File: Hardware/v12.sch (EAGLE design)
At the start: 85 parts, among them IC1 LM324D, IC2 m328p, IC3 REG1117, IC4 OPA336U, J1 22-27-2081-08, J2 22-27-2031-03

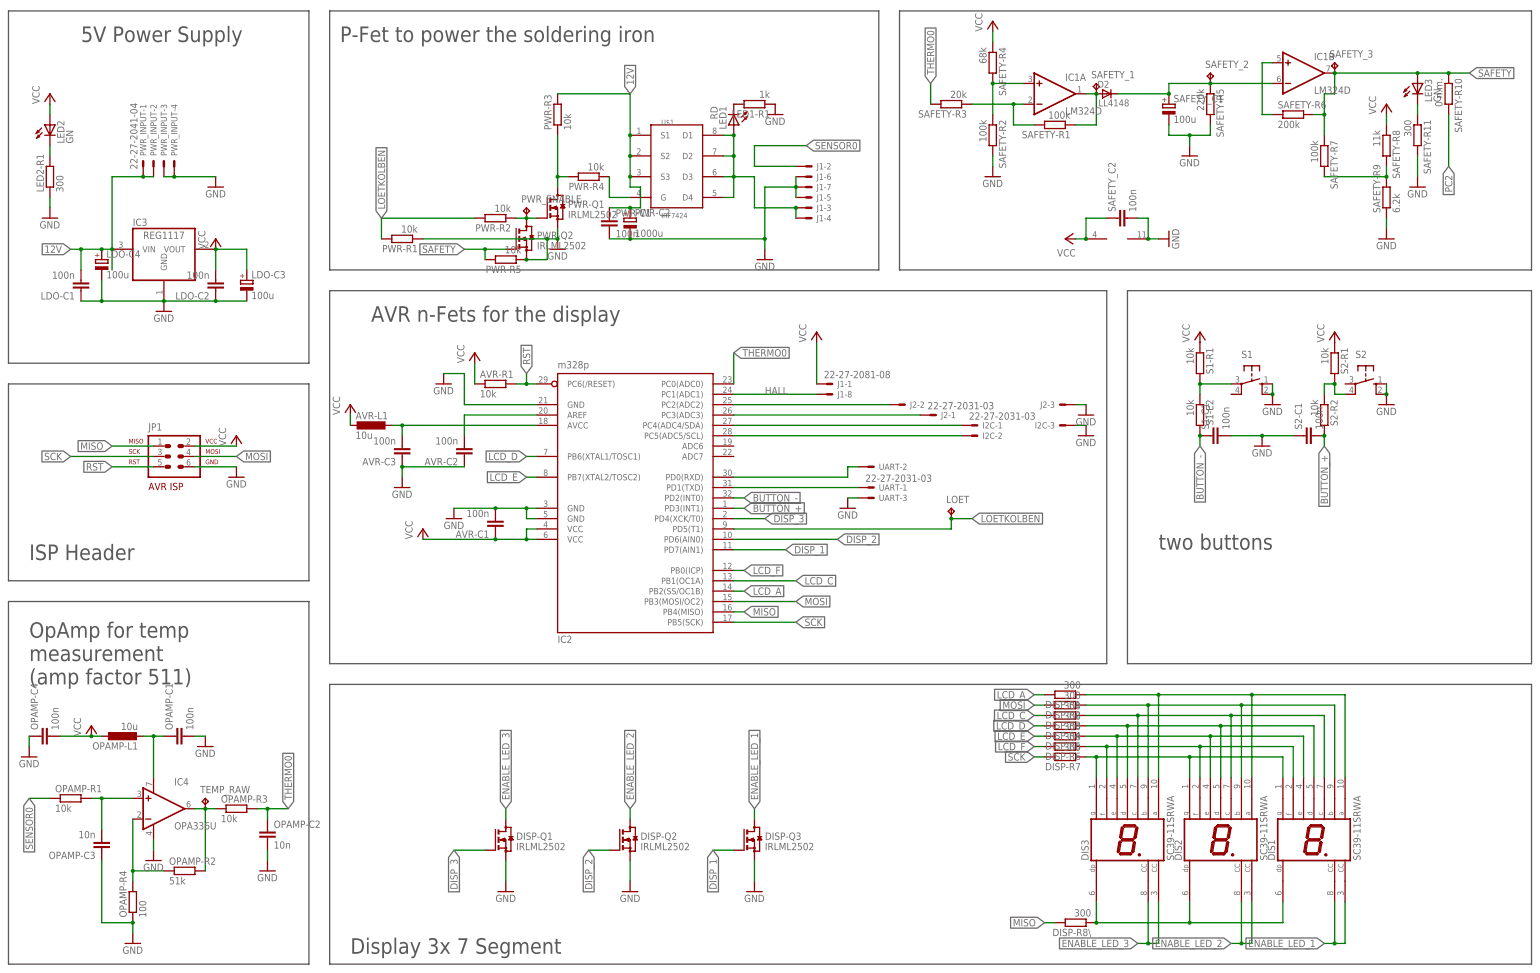
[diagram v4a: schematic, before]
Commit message: changed some values (led resistors) updated shopping list
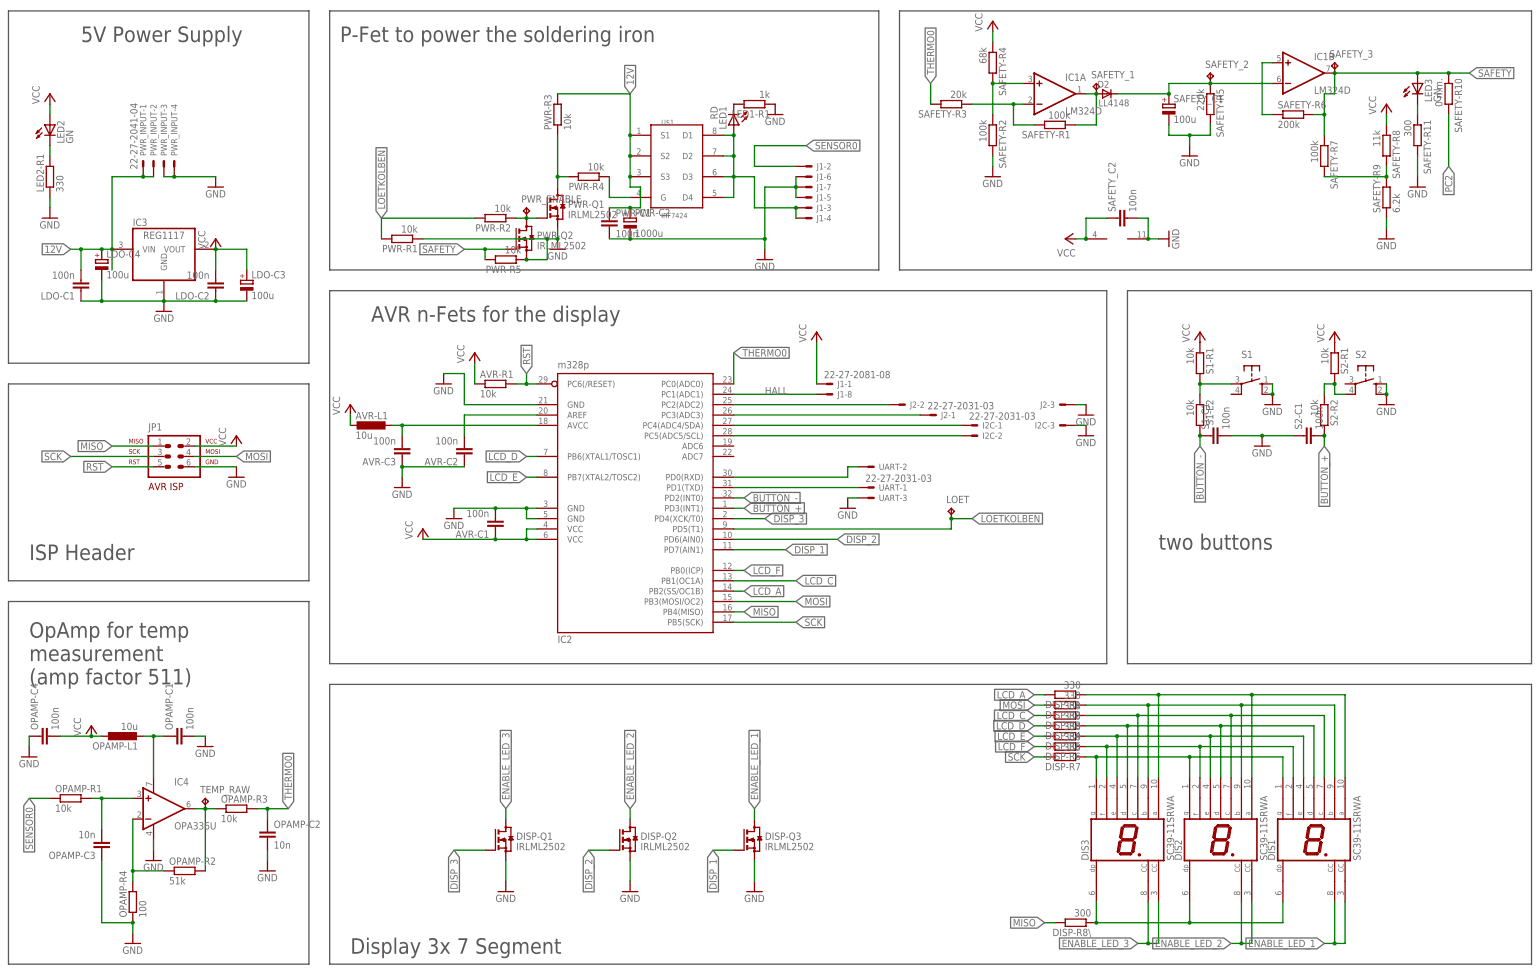
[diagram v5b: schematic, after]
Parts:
- DISP-R1, DISP-R2, DISP-R3, DISP-R4, DISP-R5, DISP-R6, DISP-R7, LED2-R1: value 300 -> 330
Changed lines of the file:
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@@
 <part name="P+8" library="supply1" deviceset="VCC" device=""/>
 <part name="LED2" library="led" deviceset="LED" device="CHIP-LED0805" value="GN"/>
-<part name="LED2-R1" library="rcl" deviceset="R-EU_" device="R0603" value="300"/>
+<part name="LED2-R1" library="rcl" deviceset="R-EU_" device="R0603" value="330"/>
 <part name="GND20" library="supply1" deviceset="GND" device=""/>
 <part name="P+9" library="supply1" deviceset="VCC" device=""/>
@@
 <part name="DIS1" library="display-hp" deviceset="SC39-11SRWA" device=""/>
 <part name="DIS3" library="display-hp" deviceset="SC39-11SRWA" device=""/>
-<part name="DISP-R7" library="rcl" deviceset="R-EU_" device="R0603" value="300"/>
-<part name="DISP-R6" library="rcl" deviceset="R-EU_" device="R0603" value="300"/>
-<part name="DISP-R5" library="rcl" deviceset="R-EU_" device="R0603" value="300"/>
-<part name="DISP-R4" library="rcl" deviceset="R-EU_" device="R0603" value="300"/>
-<part name="DISP-R3" library="rcl" deviceset="R-EU_" device="R0603" value="300"/>
-<part name="DISP-R2" library="rcl" deviceset="R-EU_" device="R0603" value="300"/>
-<part name="DISP-R1" library="rcl" deviceset="R-EU_" device="R0603" value="300"/>
+<part name="DISP-R7" library="rcl" deviceset="R-EU_" device="R0603" value="330"/>
+<part name="DISP-R6" library="rcl" deviceset="R-EU_" device="R0603" value="330"/>
+<part name="DISP-R5" library="rcl" deviceset="R-EU_" device="R0603" value="330"/>
+<part name="DISP-R4" library="rcl" deviceset="R-EU_" device="R0603" value="330"/>
+<part name="DISP-R3" library="rcl" deviceset="R-EU_" device="R0603" value="330"/>
+<part name="DISP-R2" library="rcl" deviceset="R-EU_" device="R0603" value="330"/>
+<part name="DISP-R1" library="rcl" deviceset="R-EU_" device="R0603" value="330"/>
 <part name="DISP-R8\" library="rcl" deviceset="R-EU_" device="R0603" value="300"/>
 <part name="PWR-Q2" library="transistor-small-signal" deviceset="BSS123" device="" value="IRLML2502"/>

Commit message: latest updates for finished hardware version 1.2
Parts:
- removed SAFETY-R6: 200k, rcl:R-EU_R0603
- removed SAFETY-R7: 100k, rcl:R-EU_R0603
- added R24: 100k, rcl:R-EU_R0603
- added R28: 200k, rcl:R-EU_R0603
- C14: value 100u -> 56u
- C16: value 100u -> 1u
- renumbered AVR-C1 to C12, AVR-C2 to C17, AVR-C3 to C11, AVR-L1 to L1, AVR-R1 to R34, D2 to D1, DISP-R1 to R1, DISP-R2 to R3, DISP-R3 to R8, DISP-R4 to R5, DISP-R5 to R4, DISP-R6 to R2, DISP-R7 to R7, DISP-R8\ to R6, IC1 to LM324, IC2 to AVR, IC3 to LDO, IC4 to OPA, LDO-C1 to C15, LDO-C2 to C2, LDO-C3 to C13, LDO-C4 to C14, LED1-R1 to R11, LED2-R1 to R18, LOET to TPSLDR, OPAMP-C1 to C4, OPAMP-C2 to C10, OPAMP-C3 to C5, OPAMP-C4 to C6, OPAMP-L1 to L2, OPAMP-R1 to R16, OPAMP-R2 to R17, OPAMP-R3 to R33, OPAMP-R4 to R19, PWR-C1 to C1, PWR-C2 to C3, PWR-R1 to R13, PWR-R2 to R10, PWR-R3 to R15, PWR-R4 to R14, PWR-R5 to R9, PWR_ENABLE to TPPWR, S1-C1 to C8, S1-E2 to R23, S1-R1 to R22, S2-C1 to C7, S2-R1 to R20, S2-R2 to R21, SAFETY-R1 to R35, SAFETY-R10 to R32, SAFETY-R11 to R12, SAFETY-R2 to R30, SAFETY-R3 to R31, SAFETY-R4 to R29, SAFETY-R5 to R26, SAFETY-R8 to R27, SAFETY-R9 to R25, SAFETY_1 to TPS1, SAFETY_2 to TPS2, SAFETY_3 to TPS3, SAFETY_C1 to C16, SAFETY_C2 to C9, TEMP_RAW to TPTEMP, U$1 to IRF
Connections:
- net N$12: now also R24.1, R28.1; no longer SAFETY-R6.1
- net N$14: now also R24.2; no longer SAFETY-R7.2
- net SAFETY: now also R28.2; no longer SAFETY-R6.2, SAFETY-R7.1

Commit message: last changes
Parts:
- R12, R6: value 300 -> 330
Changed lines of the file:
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@@
 <part name="R3" library="rcl" deviceset="R-EU_" device="R0603" value="330"/>
 <part name="R1" library="rcl" deviceset="R-EU_" device="R0603" value="330"/>
-<part name="R6" library="rcl" deviceset="R-EU_" device="R0603" value="300"/>
+<part name="R6" library="rcl" deviceset="R-EU_" device="R0603" value="330"/>
 <part name="PWR-Q2" library="transistor-small-signal" deviceset="BSS123" device="" value="IRLML2502"/>
 <part name="OPA" library="burr-brown" deviceset="OPA336" device="U"/>
@@
 <part name="R32" library="rcl" deviceset="R-EU_" device="R0603" value="0 n.m."/>
 <part name="LED3" library="led" deviceset="LED" device="CHIP-LED0805" value="GN"/>
-<part name="R12" library="rcl" deviceset="R-EU_" device="R0603" value="300"/>
+<part name="R12" library="rcl" deviceset="R-EU_" device="R0603" value="330"/>
 <part name="GND29" library="supply1" deviceset="GND" device=""/>
 </parts>
